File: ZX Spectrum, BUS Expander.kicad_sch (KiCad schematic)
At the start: 13 parts, among them J1 Conn_02x28_Row_Letter_First, J2 Conn_02x28_Row_Letter_First

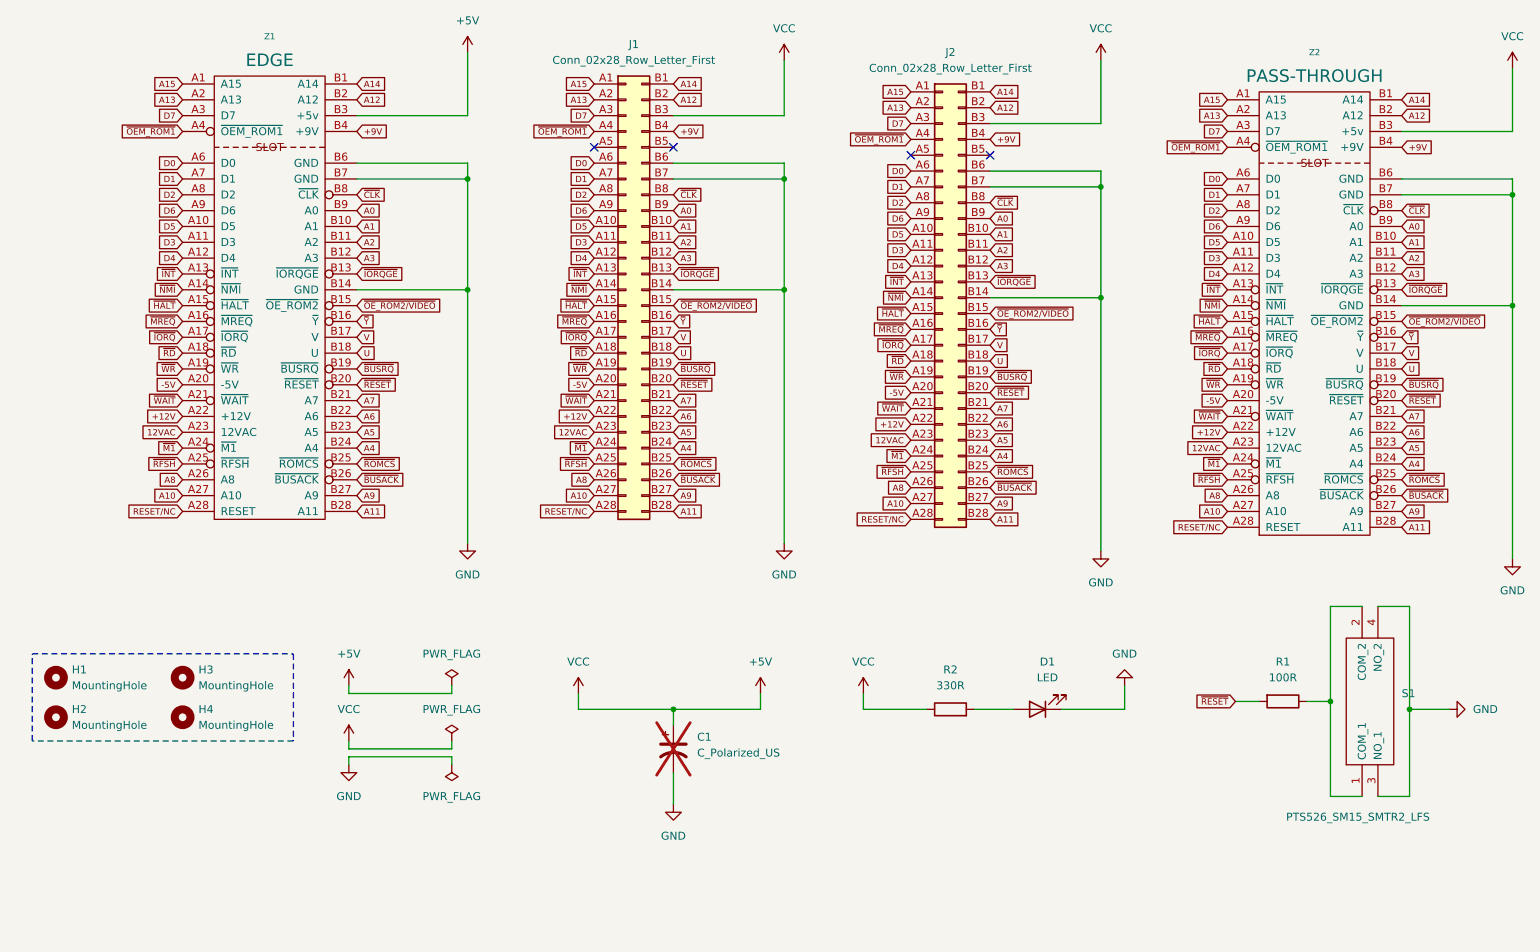
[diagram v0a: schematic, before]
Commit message: Added Nemo BUS
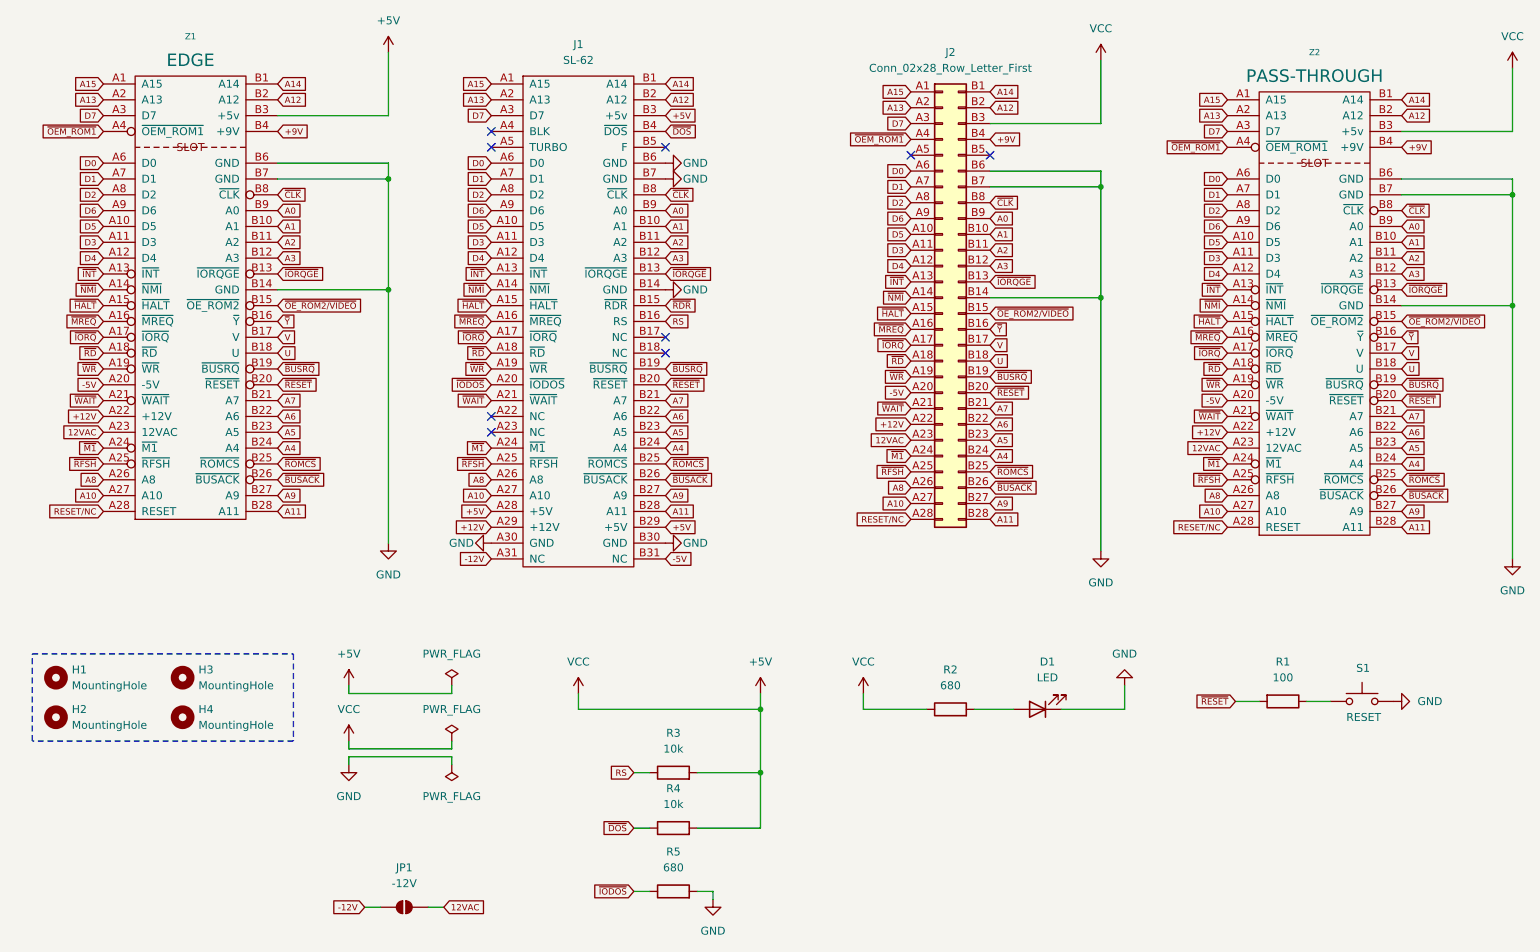
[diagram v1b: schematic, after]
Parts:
- removed C1: C_Polarized_US, Capacitor_SMD:C_1206_3216Metric, symbol Device:C_Polarized_US
- added JP1: -12V, Jumper:SolderJumper-2_P1.3mm_Open_RoundedPad1.0x1.5mm, symbol Jumper:SolderJumper_2_Open
- added R3, R4: 10k, Resistor_SMD:R_0805_2012Metric_Pad1.20x1.40mm_HandSolder, symbol Device:R
- added R5: 680, Resistor_SMD:R_0805_2012Metric_Pad1.20x1.40mm_HandSolder, symbol Device:R
- D1: footprint LED_SMD:LED_0805_2012Metric -> LED_SMD:LED_0805_2012Metric_Pad1.15x1.40mm_HandSolder
- J1: value Conn_02x28_Row_Letter_First -> SL-62; footprint My Footprint Library, Sinclair:ZX Bus Socket -> zxbus:NemoBus-SL62-inverted; symbol My Symbols_Sinclair:ZX_Spectrum,_Bus_Connector -> zxbus:NemoBus
- R1: value 100R -> 100; footprint Resistor_SMD:R_1206_3216Metric -> Resistor_SMD:R_0805_2012Metric_Pad1.20x1.40mm_HandSolder
- R2: value 330R -> 680; footprint Resistor_SMD:R_1206_3216Metric -> Resistor_SMD:R_0805_2012Metric_Pad1.20x1.40mm_HandSolder
- S1: value PTS526_SM15_SMTR2_LFS -> RESET; footprint My Footprint Library:PTS526SM15SMTR2LFS -> Button_Switch_THT:SW_PUSH_6mm; symbol My Symbols:PTS526_SM15_SMTR2_LFS -> Switch:SW_Push
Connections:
- net +12V: now also J1.A29 (+12V); no longer J1.A22 (Pin_a22)
- net +5V: now also J1.A28 (+5V), J1.B29 (+5V), R3.2, R4.2
- net +9V: no longer J1.B4 (Pin_b4)
- net -5V: now also J1.B31 (NC); no longer J1.A20 (Pin_a20)
- net 12VAC: now also JP1.2 (B); no longer J1.A23 (Pin_a23)
- net GND: now also J1.A30 (GND), J1.B30 (GND), S1.2, R5.2; no longer S1.3 (NO_1), S1.4 (NO_2)
- net RESET/NC: no longer J1.A28 (Pin_a28)
- net U: no longer J1.B18 (Pin_b18)
- net V: no longer J1.B17 (Pin_b17)
- net ~{OEM_ROM1}: no longer J1.A4 (Pin_a4)
- net ~{OE_ROM2/VIDEO}: no longer J1.B15 (Pin_b15)
- net ~{Y}: no longer J1.B16 (Pin_b16)
- net at R1.1, S1.1: no longer S1.2 (COM_2)
- new net -12V: J1.A31 (NC), JP1.1 (A)
- new net RS: J1.B16 (RS), R3.1
- new net ~{DOS}: J1.B4 (~{DOS}), R4.1
- new net ~{IODOS}: J1.A20 (~{IODOS}), R5.1
- new net ~{RDR}: J1.B15 (~{RDR})
- no-connect marks 4 -> 9
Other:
- moved on the sheet: Z1

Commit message: Fixed Nemobus romcs signal
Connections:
- net ~{RDR} is gone; now on net ~{ROMCS}: J1.B15 (~{RDR})
- net ~{ROMCS}: no longer J1.B25 (~{ROMCS})
- no-connect marks 9 -> 10
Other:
- company: (none) -> andykarpov production
- title: (none) -> ZX Spectrum Nemo Bus & ZX Bus Expander
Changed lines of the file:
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@@
 	(generator_version "8.0")
 	(paper "A4")
+	(title_block
+		(title "ZX Spectrum Nemo Bus & ZX Bus Expander")
+		(date "2024-10-22")
+		(rev "A")
+		(company "andykarpov production")
+		(comment 1 "Initial revision")
+		(comment 2 "Special Exclusive Kalantaj edition")
+	)
 	(junction
 		(at 77.47 48.26)
@@
 	)
 	(no_connect
+		(at 121.92 93.98)
+	)
+	(no_connect
 		(at 93.98 86.36)
 	)
@@
 	(global_label "~{ROMCS}"
 		(shape input)
-		(at 121.92 93.98 0)
+		(at 121.92 68.58 0)
 		(fields_autoplaced yes)
 		(effects
@@
 		)
 		(property "Intersheetrefs" "${INTERSHEET_REFS}"
-			(at 129.4132 93.98 0)
+			(at 129.4132 68.58 0)
 			(effects
 				(font
@@
 			(effects
 				(font
-					(size 1.27 1.27)
-				)
-				(justify left)
-				(hide yes)
-			)
-		)
-	)
-	(global_label "~{RDR}"
-		(shape input)
-		(at 121.92 68.58 0)
-		(fields_autoplaced yes)
-		(effects
-			(font
-				(size 1 1)
-			)
-			(justify left)
-		)
-		(property "Intersheetrefs" "${INTERSHEET_REFS}"
-			(at 127.2703 68.58 0)
-			(effects
-				(font

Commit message: Added more test points on nemobus slot
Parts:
- added JP2: ROMCS, Jumper:SolderJumper-2_P1.3mm_Bridged_RoundedPad1.0x1.5mm, symbol Jumper:SolderJumper_2_Bridged
- added TP1, TP2, TP3, TP4, TP5: TestPoint, TestPoint:TestPoint_Pad_D2.0mm, symbol Connector:TestPoint
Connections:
- net ~{ROMCS}: now also JP2.2 (B); no longer J1.B15 (~{RDR})
- net at J1.A4 (BLK): now also TP1.1
- net at J1.A5 (TURBO): now also TP2.1
- net at J1.B25 (~{ROMCS}): now also TP4.1
- net at J1.B5 (F): now also TP3.1
- new net: J1.B15 (~{RDR}), JP2.1 (A), TP5.1
- no-connect marks 10 -> 6

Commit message: Added more leds
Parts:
- added D2: +12V, LED_SMD:LED_0805_2012Metric_Pad1.15x1.40mm_HandSolder, symbol Device:LED
- added D3: -5V, LED_SMD:LED_0805_2012Metric_Pad1.15x1.40mm_HandSolder, symbol Device:LED
- added D4: -12V, LED_SMD:LED_0805_2012Metric_Pad1.15x1.40mm_HandSolder, symbol Device:LED
- added D5: +9V, LED_SMD:LED_0805_2012Metric_Pad1.15x1.40mm_HandSolder, symbol Device:LED
- added R6, R8: 1k, Resistor_SMD:R_0805_2012Metric_Pad1.20x1.40mm_HandSolder, symbol Device:R
- added R7, R9: 680, Resistor_SMD:R_0805_2012Metric_Pad1.20x1.40mm_HandSolder, symbol Device:R
- D1: value LED -> +5V
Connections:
- net +12V: now also R6.1
- net +9V: now also R9.1
- net -12V: now also R8.1
- net -5V: now also R7.1
- net GND: now also D2.1 (K), D3.2 (A), D4.2 (A), D5.1 (K)
- new net: D3.1 (K), R7.2
- new net: D5.2 (A), R9.2
- new net: D4.1 (K), R8.2
- new net: D2.2 (A), R6.2
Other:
- moved on the sheet: D1, R2
